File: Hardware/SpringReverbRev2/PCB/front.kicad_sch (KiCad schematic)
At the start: 33 parts, among them SW901 SW_SPDT_MSM, U1 TL072, U2 TL072

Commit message: Schem tidying
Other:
- moved on the sheet: C6, C7, C903, C904, R1, R12, R13, R16, R2, R20, R23, R24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

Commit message: misc corrections
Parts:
- C6, C7, C903, C904: value 100n -> 100nF
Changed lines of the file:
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@@
       (effects (font (size 1.27 1.27)) (justify left))
     )
-    (property "Value" "100n" (id 1) (at 53.086 141.4022 0)
+    (property "Value" "100nF" (id 1) (at 53.086 141.4022 0)
       (effects (font (size 1.27 1.27)) (justify left))
     )
@@
     )
     (property "Vendor" "Tayda" (id 4) (at 50.165 139.7 0)
+      (effects (font (size 1.27 1.27)) hide)
+    )
+    (property "Description" "Ceramic capacitor" (id 5) (at 50.165 139.7 0)
       (effects (font (size 1.27 1.27)) hide)
     )
@@
       (effects (font (size 1.27 1.27)) (justify left))
     )
-    (property "Value" "100n" (id 1) (at 81.026 149.0222 0)
+    (property "Value" "100nF" (id 1) (at 81.026 149.0222 0)
       (effects (font (size 1.27 1.27)) (justify left))
     )
@@
       (effects (font (size 1.27 1.27)) hide)
     )
+    (property "Description" "Ceramic capacitor" (id 5) (at 78.105 147.32 0)
+      (effects (font (size 1.27 1.27)) hide)
+    )
     (pin "1")
     (pin "2")
@@
       (effects (font (size 1.27 1.27)) (justify left))
     )
-    (property "Value" "100n" (id 1) (at 53.086 149.0222 0)
+    (property "Value" "100nF" (id 1) (at 53.086 149.0222 0)
       (effects (font (size 1.27 1.27)) (justify left))
     )
@@
     )
     (property "Vendor" "Tayda" (id 4) (at 50.165 147.32 0)
+      (effects (font (size 1.27 1.27)) hide)
+    )
+    (property "Description" "Ceramic capacitor" (id 5) (at 50.165 147.32 0)
       (effects (font (size 1.27 1.27)) hide)
     )
@@
       (effects (font (size 1.27 1.27)) (justify left))
     )
-    (property "Value" "100n" (id 1) (at 81.026 141.4022 0)
+    (property "Value" "100nF" (id 1) (at 81.026 141.4022 0)
       (effects (font (size 1.27 1.27)) (justify left))
     )
@@
       (effects (font (size 1.27 1.27)) hide)
     )
+    (property "Description" "Ceramic capacitor" (id 5) (at 78.105 139.7 0)
+      (effects (font (size 1.27 1.27)) hide)
+    )

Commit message: Backlog
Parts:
- removed H904: MountingHole, ao_tht:MountingHole_3.2mm_M3, symbol ao_symbols:MountingHole
- added H905: MountingHole, AO_tht:MountingHole_3.2mm_M3, symbol AO_symbols:MountingHole
- added LED1: LED_green, AO_tht:LED_D5.0mm, symbol AO_symbols:LED_green
- added RV905: B50k, AO_tht:Potentiometer_Alpha_16mm_Single_Vertical, symbol AO_symbols:R_POT
- C6, C7, C903, C904: footprint ao_tht:C_Disc_D3.0mm_W1.6mm_P2.50mm -> AO_tht:C_Disc_D3.0mm_W1.6mm_P2.50mm; symbol ao_symbols:C -> AO_symbols:C
- GRAF902: symbol ao_symbols:Graphic -> AO_symbols:Graphic
- H903: footprint ao_tht:MountingHole_3.2mm_M3 -> AO_tht:MountingHole_3.2mm_M3; symbol ao_symbols:MountingHole -> AO_symbols:MountingHole
- R1, R12, R13, R16, R2, R20, R21, R22, R23, R24, R25, R26, R7, R8, R9: footprint ao_tht:R_Axial_DIN0207_L6.3mm_D2.5mm_P10.16mm_Horizontal -> AO_tht:R_Axial_DIN0207_L6.3mm_D2.5mm_P10.16mm_Horizontal; symbol ao_symbols:R -> AO_symbols:R
- RV901, RV902, RV903, RV904: footprint ao_tht:Potentiometer_Alpha_16mm_Single_Vertical -> AO_tht:Potentiometer_Alpha_16mm_Single_Vertical; symbol ao_symbols:R_POT -> AO_symbols:R_POT
- SW901: footprint ao_tht:SPDT-toggle-switch-1M-series -> AO_tht:SPDT-toggle-switch-1M-series; symbol ao_symbols:SW_SPDT_MSM -> AO_symbols:SW_SPDT_MSM
- TP904, TP905, TP906: footprint ao_tht:TestPoint_THTPad_D1.5mm_Drill0.7mm -> AO_tht:TestPoint_THTPad_D1.5mm_Drill0.7mm; symbol ao_symbols:TestPoint -> AO_symbols:TestPoint
- U1, U2: footprint ao_tht:DIP-8_W7.62mm_Socket_LongPads -> AO_tht:DIP-8_W7.62mm_Socket_LongPads; symbol ao_symbols:TL072 -> AO_symbols:TL072
- VR1: footprint ao_tht:Potentiometer_Bourns_3362P_Vertical_screw_centered -> AO_tht:Potentiometer_Bourns_3362P_Vertical_screw_centered; symbol ao_symbols:R_POT_TRIM_3296W -> AO_symbols:R_POT_TRIM_3296W
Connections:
- net VAC_AN_F: now also LED1.1 (K); no longer U2.1
- new net: LED1.2 (A), U2.1
- new net MIXPOT_DRY_F: RV905.3
- new net MIXPOT_MIX_F: RV905.2
- new net MIXPOT_WET_F: RV905.1
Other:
- moved on the sheet: C6, C7, C903, C904, R1, R23, R7, RV901, RV904

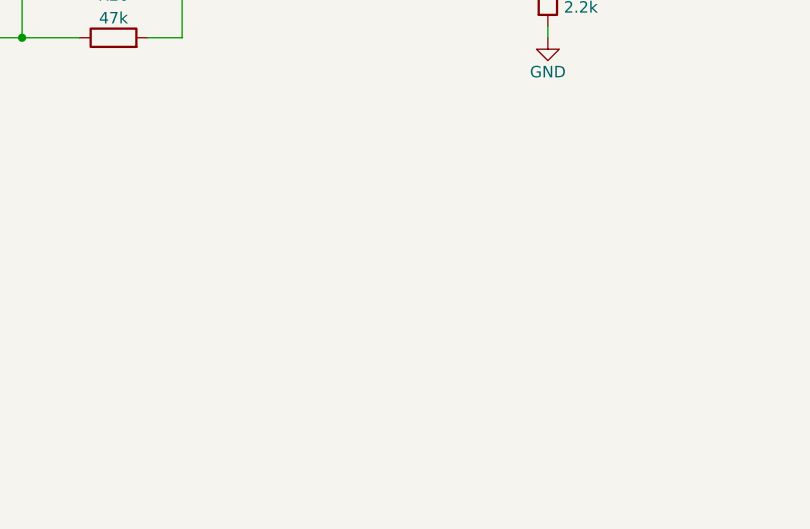
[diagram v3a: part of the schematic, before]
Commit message: Bigger tone knob; hardware
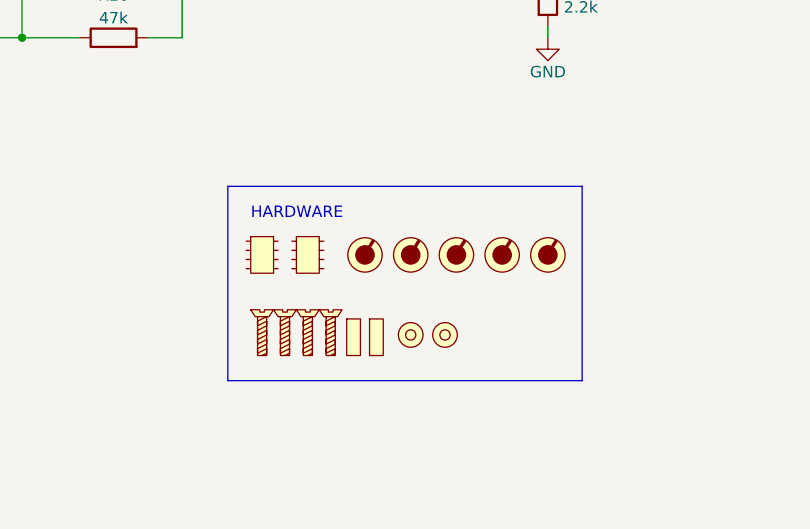
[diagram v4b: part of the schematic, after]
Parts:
- added J915, J916: DIP-8, symbol AO_symbols:DIP-8
- added ZKN901: Knob_MF-A04, symbol AO_symbols:Knob
- added ZKN902: Knob_MF-A03, symbol AO_symbols:Knob
- added ZKN903, ZKN904, ZKN905: Knob_MF-A01, symbol AO_symbols:Knob
- added ZSC901, ZSC902, ZSC903, ZSC904: Screw, symbol AO_symbols:Screw
- added ZSP901, ZSP902: Spacer, symbol AO_symbols:Spacer
- added ZWA901, ZWA902: Washer, symbol AO_symbols:Washer
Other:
- note added: "HARDWARE"
